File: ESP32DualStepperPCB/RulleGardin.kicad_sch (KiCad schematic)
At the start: 13 parts, among them J1 Power, J3 Conn_01x05, U2 TSR_1-2433, U3 ULN2003A, U4 AZ1117-3.3

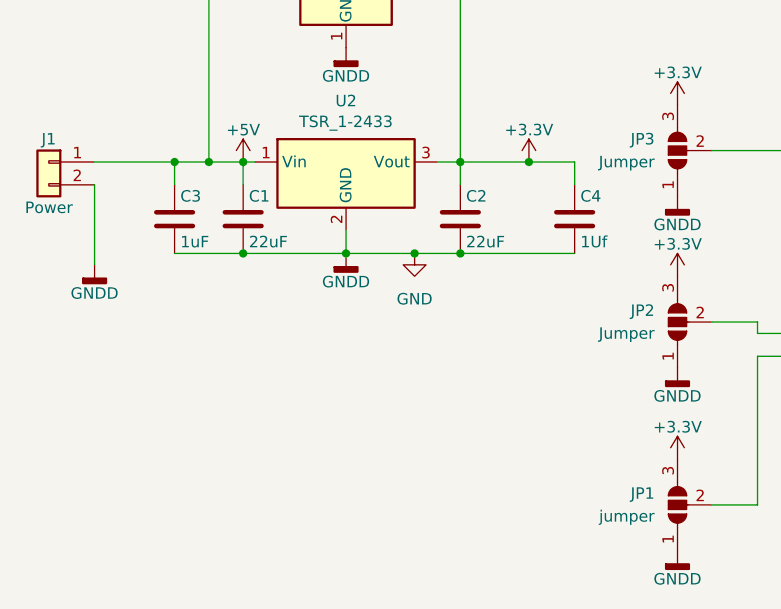
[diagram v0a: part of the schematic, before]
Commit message: fund that its the dhcp that the problem, so now with static IP
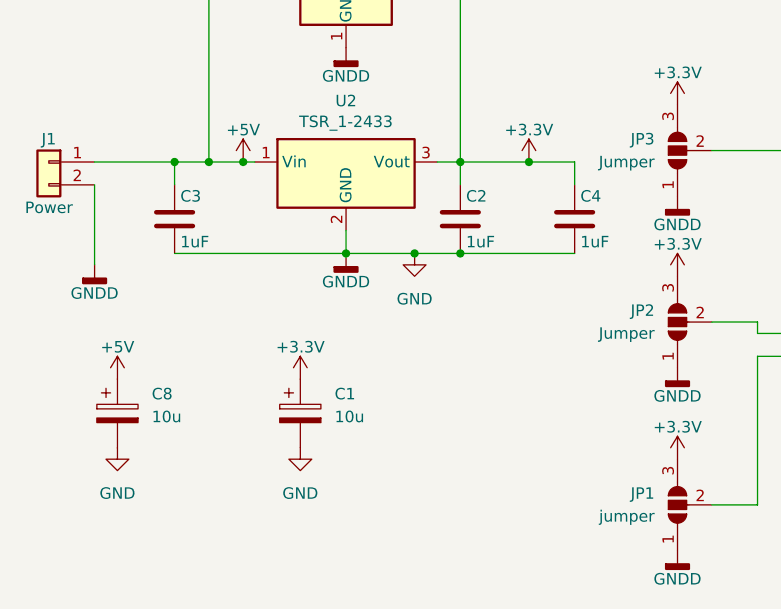
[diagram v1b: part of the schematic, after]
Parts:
- removed C1: 22uF, Capacitor_SMD:C_0805_2012Metric, symbol Device:C
- added C1: 10u, Capacitor_SMD:CP_Elec_4x5.4, symbol Device:C_Polarized
- added C8: 10u, Capacitor_SMD:CP_Elec_6.3x7.7, symbol Device:C_Polarized
- C2: value 22uF -> 1uF; footprint Capacitor_SMD:C_0805_2012Metric -> Capacitor_SMD:C_0603_1608Metric
- C3: footprint Capacitor_SMD:C_0805_2012Metric -> Capacitor_SMD:C_0603_1608Metric
- C4: value 1Uf -> 1uF; footprint Capacitor_SMD:C_0805_2012Metric -> Capacitor_SMD:C_0603_1608Metric
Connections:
- net +3.3V: now also C1.1
- net +5V: now also C8.1
- net GND: now also C1.2, C8.2

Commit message: med device understøttelse
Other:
- sheet ESP32: file StdEsp32.kicad_sch -> StdEsp32_worm32.kicad_sch
- sheet ESP32 ports: added GPIO19, GPIO21, GPIO25, GPIO26, GPIO27, GPIO32, GPIO33, GPIO34, SCL, SDA, Uart2_RX, Uart2_TX; removed GPIO10, GPIO11, GPIO37, GPIO38, GPIO40, GPIO6, GPIO7, GPIO8, GPIO9
- note added: "Stepper Nema23"
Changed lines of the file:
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@@
 		)
 	)
+	(text "Stepper Nema23"
+		(exclude_from_sim no)
+		(at 220.472 133.35 0)
+		(effects
+			(font
+				(size 1.27 1.27)
+			)
+			(href "https://www.omc-stepperonline.com/download/23HS30-2804S.pdf?srsltid=AfmBOoofIwib1wgYiFYHcjm5GWBSbCCiXzbK5KRu2vmqnPUWyFy4xIbc")
+		)
+	)
 	(text "Common"
 		(exclude_from_sim no)
@@
 			"AAAAAAAAAAAAAAAAAAAAAAAAAAAAAAAAAAAAAAAAAAAAAAAAAAAAAAAAAAAAAAAAAAAAAAAAAAAA"
 			"AAAAAAAAAAAAAAAAAAAAAAAAAAAAAAAAAAAAAAAAAAAAAAAAAAAAAAAAAAAAAAAAAAAAAAAAAAAA"
-			"AAAAAAAAAAAAAAAAAA=="
+			"AAAAAAAAAAAAAAAAAAAAAAAAAAAAAAAAAAAAAAAAAAAAAAAAAAAAAAAAAAAAAAAAAAAAAAAAAAAA"
+			"AAAAAAAAAAAAAAAAAAAAAAAAAAAAAAAAAAAAAAAAAAAAAAAAAAAAAAAAAAAAAAAAAAAAAAAAAAAA"
+			"AAAAAAAAAAAAAAAAAAAAAAAAAAAAAAAAAAAAAAAAAAAAAAAAAAAAAAAAAAAAAAAAAAAAAAAAAAAA"
+			"AAAAAAAAAAAAAAAAAAAAAAAAAAAAAAAAAAAAAAAAAAAAAAAAAAAAAAAAAAAAAAAAAAAAAAAAAAAA"
+			"AAAAAAAAAAAAAAAAAAAAAAAAAAAAAAAAAAAAAAAAAAAAAAAAAAAAAAAAAAAAAAAAAAAAAAAAAAAA"
+			"AAAAAAAAAAAAAAAAAAAAAAAAAAAAAAAAAAAAAAAAAAAAAAAAAAAAAAAAAAAAAAAAAAAAAAAAAAAA"
+			"AAAAAAAAAAAAAAAAAAAAAAAAAAAAAAAAAAAAAAAAAAAAAAAAAAAAAAAAAAAAAAAAAAAAAAAAAAAA"
+			"AAAAAAAAAAAAAAAAAAAAAAAAAAAAAAAAAAAAAAAAAAAAAAAAAAAAAAAAAAAAAAAAAAAAAAAAAAAA"
+			"AAAAAAAAAAAAAAAAAAAAAAAAAAAAAAAAAAAAAAAAAAAAAAAAAAAAAAAAAAAAAAAAAAAAAAAAAAAA"
+			"AAAAAAAAAAAAAAAAAAAAAAAAAAAAAAAAAAAAAAAAAAAAAAAAAAAAAAAAAAAAAAAAAAAAAAAAAAAA"
+			"AAAAAAAAAAAAAAAAAAAAAAAAAAAAAAAAAAAAAAAAAAAAAAAAAAAAAAAAAAAAAAAAAAAAAAAAAAAA"
+			"AAAAAAAAAAAAAAAAAAAAAAAAAAAAAAAAAAAAAAAAAAAAAAAAAAAAAAAAAAAAAAAAAAAAAAAAAAAA"
+			"AAAAAAAAAAAAAAAAAAAAAAAAAAAAAAAAAAAAAAAAAAAAAAAAAAAAAAAAAAAAAAAAAAAAAAAAAAAA"
+			"AAAAAAAAAAAAAAAAAAAAAAAAAAAAAAAAAAAAAAAAAAAAAAAAAAAAAAAAAAAAAAAAAAAAAAAAAAAA"
+			"AAAAAAAAAAAAAAAAAAAAAAAAAAAAAAAAAAAAAAAAAAAAAAAAAAAAAAAAAAAAAAAAAAAAAAAAAAAA"
+			"AAAAAAAAAAAAAAAAAAAAAAAAAAAAAAAAAAAAAAAAAAAAAAAAAAAAAAAAAAAAAAAAAAAAAAAAAAAA"
+			"AAAAAAAAAAAAAAAAAAAAAAAAAAAAAAAAAAAAAAAAAAAAAAAAAAAAAAAAAAAAAAAAAAAAAAAAAAAA"
+			"AAAAAAAAAAAAAAAAAAAAAAAAAAAAAAAAAAAAAAAAAAAAAAAAAAAAAAAAAAAAAAAAAAAAAAAAAAAA"
+			"AAAAAAAAAAAAAAAAAABpAGIAbABlACAAIAAgACAAIAAgACAAIAAgACAAPQAgACIAdAByAHUAZQAi"
+			"AA0ADQAKAGEAYwBjAHIAbwBsAGUAIAAgACAAIAAgACAAIAAgACAAIAAgACAAIAA9ACAAIgBzAHQA"
+			"YQB0AGkAYwB0AGUAeAB0ACIADQANAAoALwA+AA0ADQAKADwALwBpAGYAPgANAA0ACgA8AGkAZgAg"
+			"AGkAZAA9ACIAYQB0AG8AbQAoAEUAeABwAGEAbgBkAGUAZABGAG8AbwB0AGUAcgBUAGUAeAB0AEwA"
+			"aQBuAGsAKQAiAD4ADQANAAoAPABjAGMAcwB5AHMAbABpAG4AawANAA0ACgBmAG8AbgB0ACAAIAAg"
+			"ACAAIAAgACAAIAAgACAAIAAgACAAIAAgACAAPQAgACIAZwB0AGYAKABUAGEAcwBrAEQAaQBhAGwA"
+			"bwBnAFMAdAB5AGwAZQAsACAAMQA4ACwAIAAwACkAIgANAA0ACgBmAG8AcgBlAGcAcgBvAHUAbgBk"
+			"ACAAIAAgACAAIAAgACAAIAAgACAAPQAgACIAZwB0AGMAKABUAGEAcwBrAEQAaQBhAGwAbwBnAFMA"
+			"dAB5AGwAZQAsACAAMQA4ACwAIAAwACwAIAAzADgAMAAzACkAIgANAA0ACgAvAD4ADQANAAoAPAAv"
+			"AGkAZgA+AA0ADQAKADwALwBzAHQAeQBsAGUAPgANAA0ACgA8AC8AcwB0AHkAbABlAHMAaABlAGUA"
+			"dABzAD4ADQANAAoAPAAvAGQAdQBpAHgAbQBsAD4ADQANAAoARTsKU0VRLkYgUgAAAAAAAAAAmAB+"
+			"3/8BAAAwLCAwfTsKVEcAAEeIVCsAsL5z5P8BAADgUljg/wEAAEUueDsKRERYLkYzMiBSMC54eSwg"
+			"ZnJhZ21lbnQuYXR0cmliWzBdLnl6enc7CkRQMi5GMzIgUjAudywgUjAsIFIwOwpSU1EuRjMyIFIx"
+			"LngsIFIwLnc7CkkyRi5TIFIwLncsIGNbMV0ueDsKRElWLkYzMiBSMS55LCBSMC53LCBSMS54OwpQ"
+			"SzY0LlUgRDAueCwgY1swXTsKVEVYLkYgUjAueHl6LCBmcmFnbWVudC5hdHRyaWJbMF0ueXp6dywg"
+			"aGFuZGxlKEQwLngpLCAyRDsKTUFYLkYgUjEueCwgUjAsIFIwLnk7Ck1JTi5GIFIwLngsIFIwLCBS"
+			"MC55OwpNSU4uRiBSMC56LCBSMCwgUjEueDsKTUFELkYzMiBSMC53LCAtUjEueSwgezAuMjUsIDAu"
+			"NSwgMCwgMH0ueCwgezAuMjUsIDAuNSwgMCwgMH0ueTsKTUFELkYzMiBSMS54LCBSMS55LCB7MC4y"
+			"NSwgMCwgMCwgMH0sIA=="
 		)
 	)
@@
 			)
 		)
-		(property "Sheetfile" "StdEsp32.kicad_sch"
+		(property "Sheetfile" "StdEsp32_worm32.kicad_sch"
 			(at 109.22 102.1846 0)
 			(effects
@@
 			)
 		)
-		(pin "EN" input
-			(at 109.22 49.53 180)
-			(effects
-				(font
-					(size 1.27 1.27)
-				)
-				(justify left)
-			)
-		)
 		(pin "GPIO0" input
 			(at 135.89 91.44 0)
@@
 			)
 		)
-		(pin "GPIO6" input
-			(at 109.22 78.74 180)
+		(pin "EN" input
+			(at 109.22 48.26 180)
 			(effects
 				(font
@@
 			)
 		)
-		(pin "GPIO7" input
-			(at 109.22 81.28 180)
+		(pin "GPIO12" input
+			(at 109.22 52.07 180)
 			(effects
 				(font
@@
 			)
 		)
-		(pin "GPIO8" input
-			(at 109.22 83.82 180)
+		(pin "GPIO13" input
+			(at 109.22 54.61 180)
 			(effects
 				(font
@@
 			)
 		)
-		(pin "GPIO9" input
-			(at 109.22 86.36 180)
+		(pin "GPIO14" input
+			(at 109.22 57.15 180)
 			(effects
 				(font
@@
 			)
 		)
-		(pin "GPIO10" input
-			(at 109.22 88.9 180)
+		(pin "GPIO15" input
+			(at 109.22 59.69 180)
 			(effects
 				(font
@@
 			)
 		)
-		(pin "GPIO11" input
-			(at 109.22 91.44 180)
+		(pin "GPIO16" input
+			(at 109.22 62.23 180)
 			(effects
 				(font
@@
 			)
 		)
-		(pin "GPIO12" input
-			(at 109.22 93.98 180)
+		(pin "GPIO17" input
+			(at 109.22 64.77 180)
 			(effects
 				(font
@@
 			)
 		)
-		(pin "GPIO13" input
-			(at 109.22 53.34 180)
+		(pin "GPIO18" input
+			(at 109.22 67.31 180)
 			(effects
 				(font
@@
 			)
 		)
-		(pin "GPIO14" input
-			(at 109.22 55.88 180)
+		(pin "GPIO19" input
+			(at 109.22 69.85 180)
 			(effects
 				(font
@@
 			)
 		)
-		(pin "GPIO15" input
-			(at 109.22 58.42 180)
+		(pin "GPIO21" input
+			(at 109.22 72.39 180)
 			(effects
 				(font
@@
 			)
 		)
-		(pin "GPIO16" input
-			(at 109.22 60.96 180)
+		(pin "GPIO25" input
+			(at 109.22 74.93 180)
 			(effects
 				(font
@@
 			)
 		)
-		(pin "GPIO17" input
-			(at 109.22 63.5 180)
+		(pin "GPIO26" input
+			(at 109.22 77.47 180)
 			(effects
 				(font
@@
 			)
 		)
-		(pin "GPIO18" input
-			(at 109.22 66.04 180)
+		(pin "GPIO27" input
+			(at 109.22 80.01 180)
 			(effects
 				(font
@@
 			)
 		)
-		(pin "GPIO35" input
-			(at 109.22 68.58 180)
+		(pin "GPIO32" input
+			(at 109.22 82.55 180)
 			(effects
 				(font
@@
 			)
 		)
-		(pin "GPIO37" input
-			(at 109.22 71.12 180)
+		(pin "GPIO33" input
+			(at 109.22 85.09 180)
 			(effects
 				(font
@@
 			)
 		)
-		(pin "GPIO38" input
-			(at 109.22 73.66 180)
+		(pin "GPIO34" input
+			(at 109.22 87.63 180)
 			(effects
 				(font
@@
 			)
 		)
-		(pin "GPIO40" input
-			(at 109.22 76.2 180)
+		(pin "GPIO35" input
+			(at 109.22 90.17 180)
 			(effects
 				(font
@@
 		)
 		(pin "RX" input
-			(at 109.22 96.52 180)
+			(at 109.22 92.71 180)
+			(effects
+				(font
+					(size 1.27 1.27)
+				)
+				(justify left)
+			)
+		)
+		(pin "SCL" input
+			(at 109.22 95.25 180)
+			(effects
+				(font
+					(size 1.27 1.27)
+				)
+				(justify left)
+			)
+		)
+		(pin "SDA" input
+			(at 109.22 97.79 180)
 			(effects
 				(font
@@
 			)
 		)
+		(pin "Uart2_RX" input
+			(at 135.89 52.07 0)
+			(effects
+				(font
+					(size 1.27 1.27)
+				)
+				(justify right)
+			)
+		)
+		(pin "Uart2_TX" input
+			(at 135.89 54.61 0)
+			(effects
+				(font
+					(size 1.27 1.27)
+				)
+				(justify right)
+			)
+		)
